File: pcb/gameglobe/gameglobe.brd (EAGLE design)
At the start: 99.1 x 49.5 mm, 14 parts

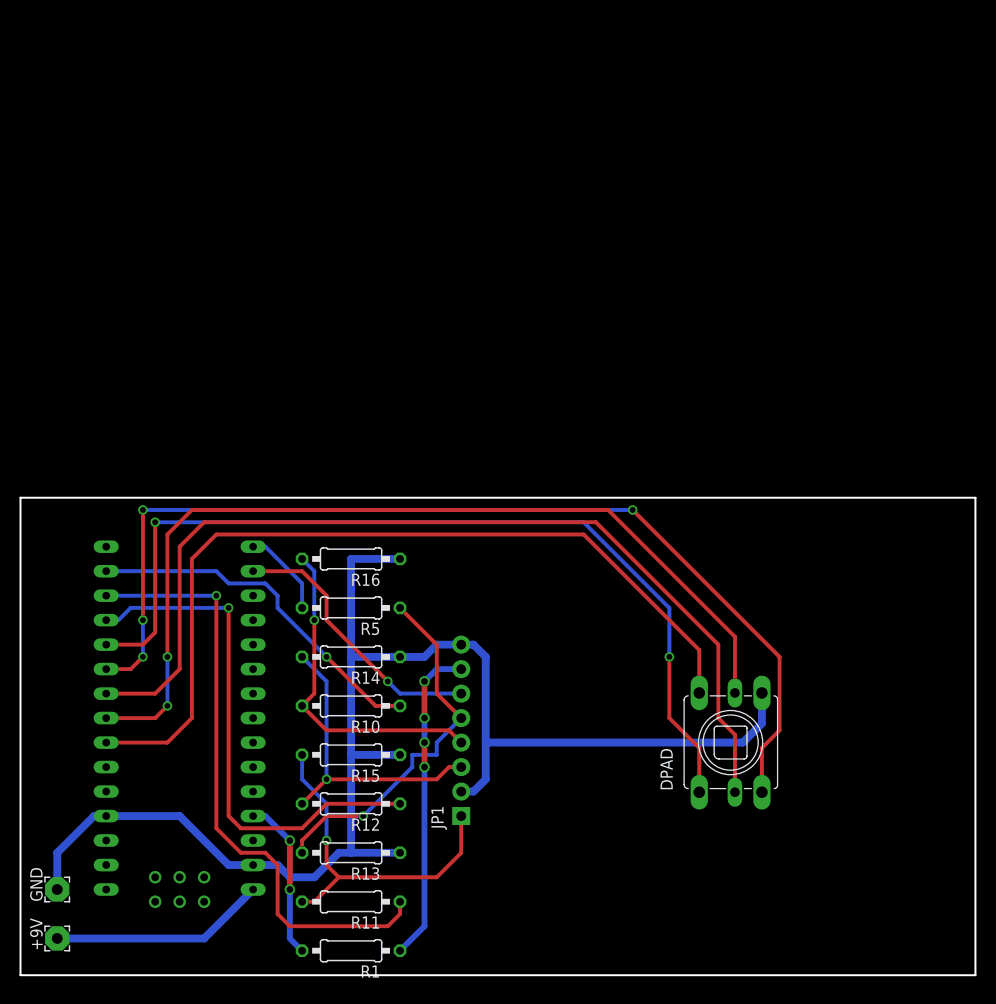
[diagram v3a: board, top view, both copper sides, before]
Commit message: Updated DRU file; Improved PCB layout; Added rounded edges and mount holes
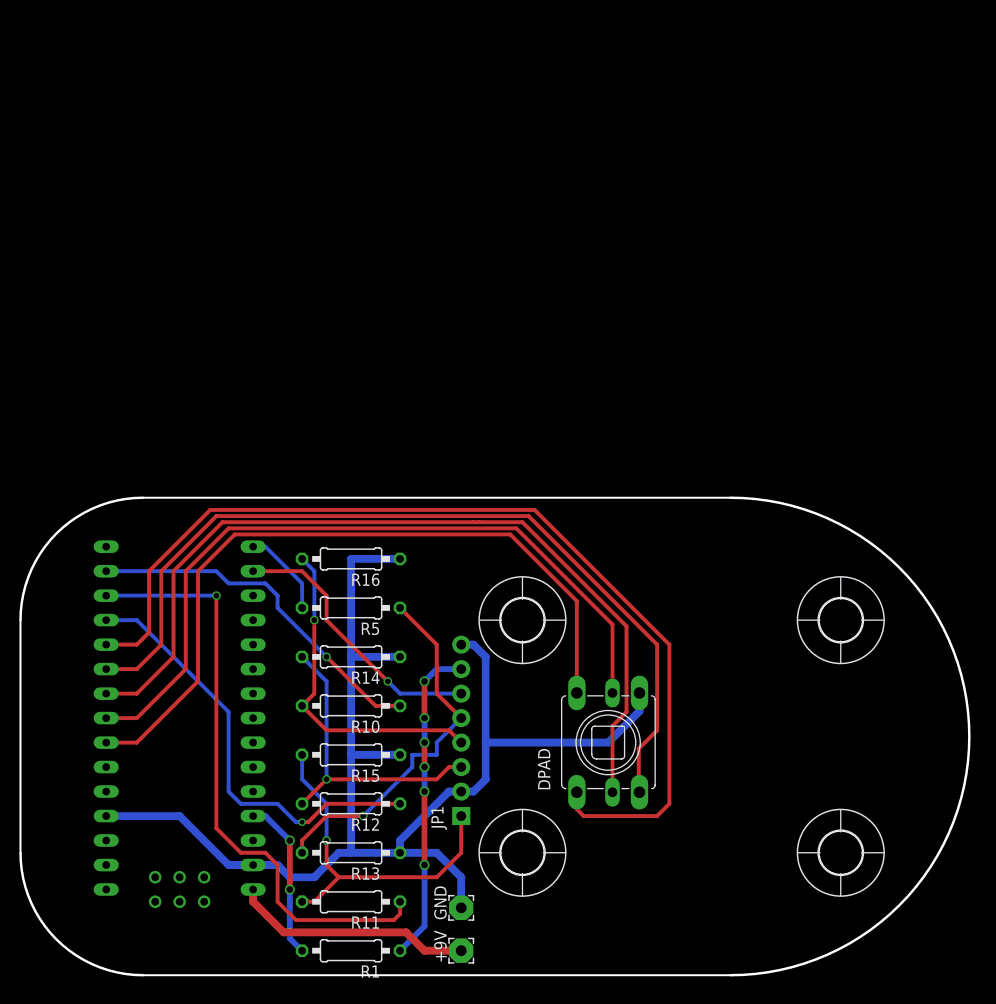
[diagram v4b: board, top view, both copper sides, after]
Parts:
- added ARDUINO_NANO: NANO, Arduino-clone:NANO
- added U$2, U$3, U$4: (no value), holes:4,5
- U$1: value NANO -> (none); device Arduino-clone:NANO -> holes:4,5
- moved GND 42.0 mm to (45.7, 6.99)
- moved +9V 41.9 mm to (45.7, 2.54)
- moved U$1 38.4 mm to (52.1, 12.7), flipped to the top
- moved DPAD 12.7 mm to (61.0, 24.1)
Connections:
- net DPAD_CENTER: now also ARDUINO_NANO.D4; no longer U$1.D4
- net DPAD_DOWN: now also ARDUINO_NANO.D7; no longer U$1.D7
- net DPAD_LEFT: now also ARDUINO_NANO.D6; no longer U$1.D6
- net DPAD_RIGHT: now also ARDUINO_NANO.D5; no longer U$1.D5
- net DPAD_UP: now also ARDUINO_NANO.D8; no longer U$1.D8
- net GND: now also ARDUINO_NANO.GND, ARDUINO_NANO.GND1; no longer U$1.GND, U$1.GND1
- net LCD_VCC: now also ARDUINO_NANO.3.3V; no longer U$1.3.3V
- net N$1: now also ARDUINO_NANO.D13; no longer U$1.D13
- net N$11: now also ARDUINO_NANO.5V; no longer U$1.5V
- net N$2: now also ARDUINO_NANO.D11; no longer U$1.D11
- net N$3: now also ARDUINO_NANO.D10; no longer U$1.D10
- net N$4: now also ARDUINO_NANO.D9; no longer U$1.D9
- net N$7: now also ARDUINO_NANO.RAW; no longer U$1.RAW
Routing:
- net DPAD_RIGHT: track 95.9 -> 77.9 mm, vias 2 -> 0
- net DPAD_DOWN: track 106.7 -> 89.8 mm, vias 4 -> 0
- net DPAD_CENTER: track 89.6 -> 76.9 mm
- net DPAD_LEFT: track 99.6 -> 88.8 mm
- net GND: track 148.7 -> 138.2 mm
- net N$4: track 54.2 -> 44.8 mm
- net DPAD_UP: track 94.5 -> 102.4 mm, vias 2 -> 0
- net N$7: track 22.4 -> 25.0 mm
- net N$3: track 63.6 -> 62.3 mm
- net LCD_LED: vias 4 -> 6
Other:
- board size 99.1 x 49.5 mm -> 98.4 x 49.5 mm
- board text added: "9V Battery"

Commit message: More PCB improvements, moved the Nano a bit sideways and improved battery mounting holes
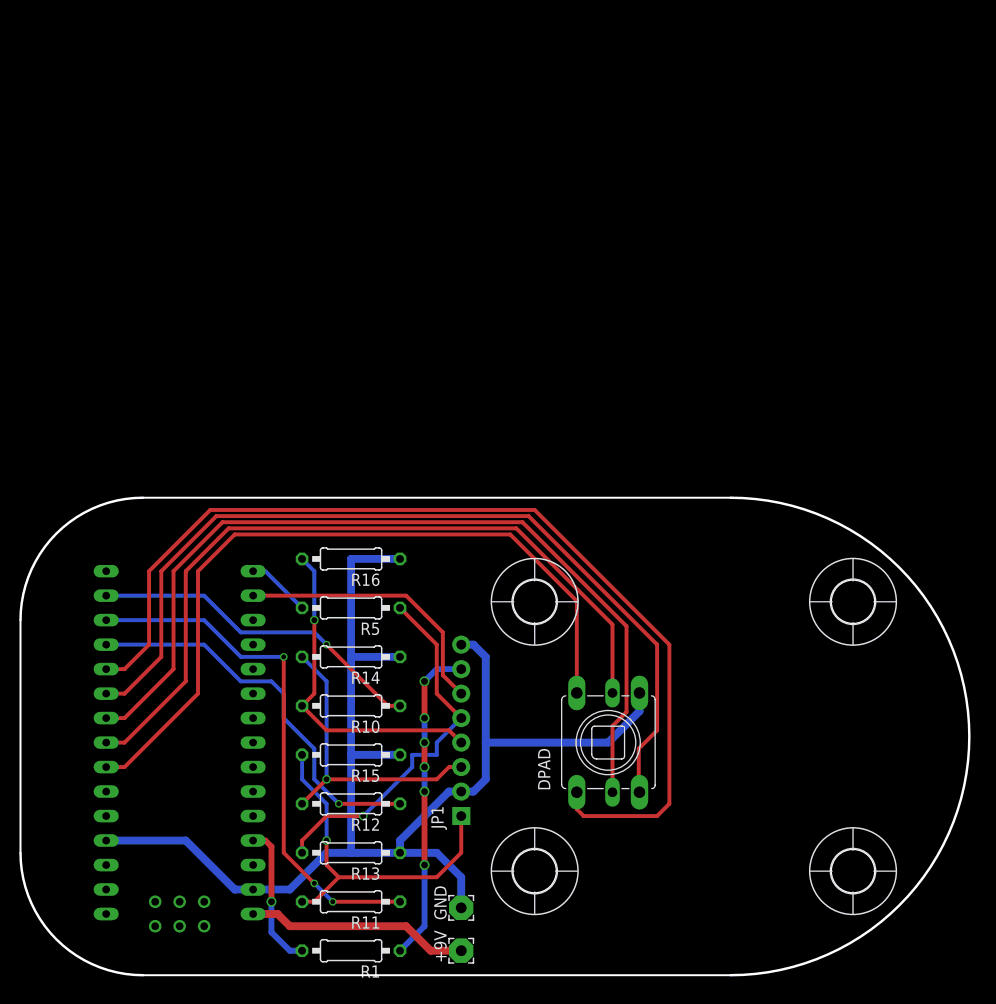
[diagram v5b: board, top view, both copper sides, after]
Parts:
- moved ARDUINO_NANO 2.54 mm to (14.0, 15.2)
- moved U$2 2.29 mm to (53.3, 38.7)
- moved U$1 2.29 mm to (53.3, 10.8)
- moved U$4 2.29 mm to (86.4, 38.7)
- moved U$3 2.29 mm to (86.4, 10.8)
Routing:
- net N$3: track 62.3 -> 54.5 mm, vias 1 -> 3
- net N$4: track 44.8 -> 40.7 mm
- net N$1: track 9.20 -> 6.66 mm
- net DPAD_UP: track 102.4 -> 104.2 mm
- net DPAD_RIGHT: track 77.9 -> 79.7 mm
- net DPAD_CENTER: track 76.9 -> 78.6 mm
- net N$7: track 25.0 -> 23.2 mm
- net N$11: track 16.8 -> 15.0 mm, vias 2 -> 1
- net DPAD_LEFT: track 88.8 -> 90.6 mm
- net DPAD_DOWN: track 89.8 -> 91.6 mm
- net N$2: track 37.0 -> 35.2 mm
- net LCD_VCC: track 28.3 -> 28.4 mm, vias 1 -> 0

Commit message: Many PCB improvements. Actually the first version where everything (joystick, lcd, nano) is centered on the board
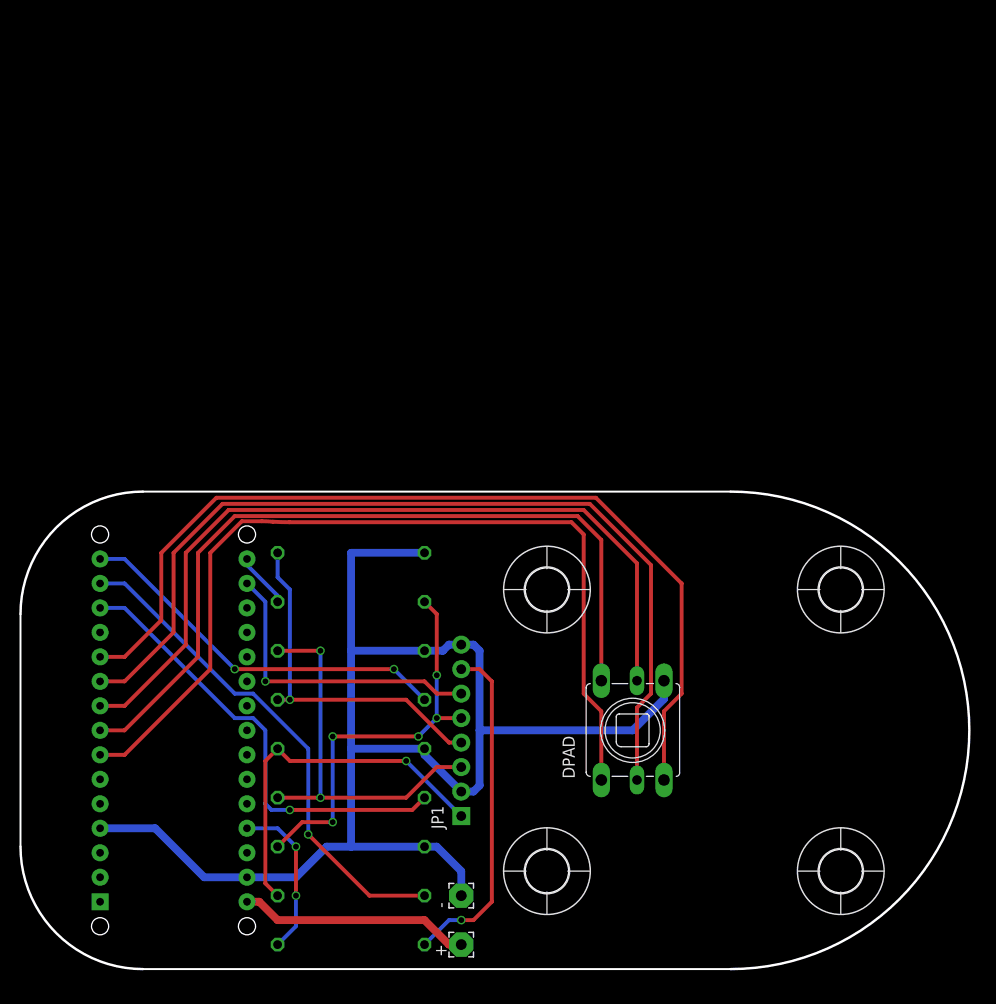
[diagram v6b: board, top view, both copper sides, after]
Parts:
- removed +9V, GND: WIREPAD2,54/1,1, wirepad:2,54/1,1
- removed ARDUINO_NANO: NANO, Arduino-clone:NANO
- added +, -: WIREPAD2,54/1,1, wirepad:2,54/1,1
- added U$5: ARDUINONANO, jet-lib:PDIP-32
- R1, R10, R11, R12, R13, R14, R15, R16, R5: device resistor:0207/10 -> resistor:0411/15
- moved DPAD 2.84 mm to (63.5, 25.4)
- moved U$2 1.80 mm to (54.6, 40.0)
- moved U$4 1.80 mm to (85.1, 40.0)
- moved U$1 1.27 mm to (54.6, 10.8)
- moved U$3 1.27 mm to (85.1, 10.8)
- moved R13 0.64 mm to (34.3, 13.3), flipped to the bottom, turned to 0 degrees
- moved R15 0.64 mm to (34.3, 23.5), flipped to the bottom, turned to 0 degrees
- moved R11 0.64 mm to (34.3, 8.26), flipped to the bottom, turned to 0 degrees
- moved R1 0.63 mm to (34.3, 3.17), flipped to the bottom, turned to 0 degrees
- moved R10 0.63 mm to (34.3, 28.6), flipped to the bottom, turned to 0 degrees
- moved R12 0.63 mm to (34.3, 18.4), flipped to the bottom, turned to 0 degrees
- moved R14 0.63 mm to (34.3, 33.7), flipped to the bottom, turned to 0 degrees
- moved R16 0.63 mm to (34.3, 43.8), flipped to the bottom, turned to 0 degrees
- moved R5 0.63 mm to (34.3, 38.7), flipped to the bottom, turned to 0 degrees
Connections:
- removed net DPAD_DOWN: ARDUINO_NANO.D7, DPAD.DOWN
- removed net DPAD_UP: ARDUINO_NANO.D8, DPAD.UP
- removed net LCD_VCC: ARDUINO_NANO.3.3V, JP1.6
- removed net N$11: ARDUINO_NANO.5V, R1.2
- new net 3V3: JP1.6, U$5.3V3
- new net 5V: R1.2, U$5.+5V
- new net N$5: DPAD.DOWN, U$5.D8
- new net N$6: DPAD.UP, U$5.D4
- net DPAD_CENTER: now also U$5.D5; no longer ARDUINO_NANO.D4
- net DPAD_LEFT: now also U$5.D7; no longer ARDUINO_NANO.D6
- net DPAD_RIGHT: now also U$5.D6; no longer ARDUINO_NANO.D5
- net GND: now also -.1, U$5.GND, U$5.GND1; no longer ARDUINO_NANO.GND, ARDUINO_NANO.GND1, GND.1
- net N$1: now also U$5.D13; no longer ARDUINO_NANO.D13
- net N$2: now also U$5.D12; no longer ARDUINO_NANO.D11
- net N$3: now also U$5.D11; no longer ARDUINO_NANO.D10
- net N$4: now also U$5.D10; no longer ARDUINO_NANO.D9
- net N$7: now also +.1, U$5.VIN; no longer +9V.1, ARDUINO_NANO.RAW
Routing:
- net DPAD_UP: track 104.2 -> 0.00 mm
- net N$5: track 0.00 -> 96.1 mm
- net N$6: track 0.00 -> 94.0 mm
- net DPAD_DOWN: track 91.6 -> 0.00 mm
- net 3V3: track 0.00 -> 31.8 mm, vias 0 -> 1
- net LCD_VCC: track 28.4 -> 0.00 mm
- net 5V: track 0.00 -> 16.8 mm, vias 0 -> 2
- net N$11: track 15.0 -> 0.00 mm, vias 1 -> 0
- net GND: track 138.2 -> 148.6 mm
- net LCD_DC: track 31.8 -> 40.1 mm, vias 1 -> 2
- net N$4: track 40.7 -> 47.3 mm
- net DPAD_LEFT: track 90.6 -> 95.1 mm
- net DPAD_CENTER: track 78.6 -> 83.2 mm
- net DPAD_RIGHT: track 79.7 -> 84.2 mm
- net N$2: track 35.2 -> 39.7 mm, vias 1 -> 2
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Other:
- board text added: "Arduino Nano"

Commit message: Fix and add own arduino Improve silkscreen texts
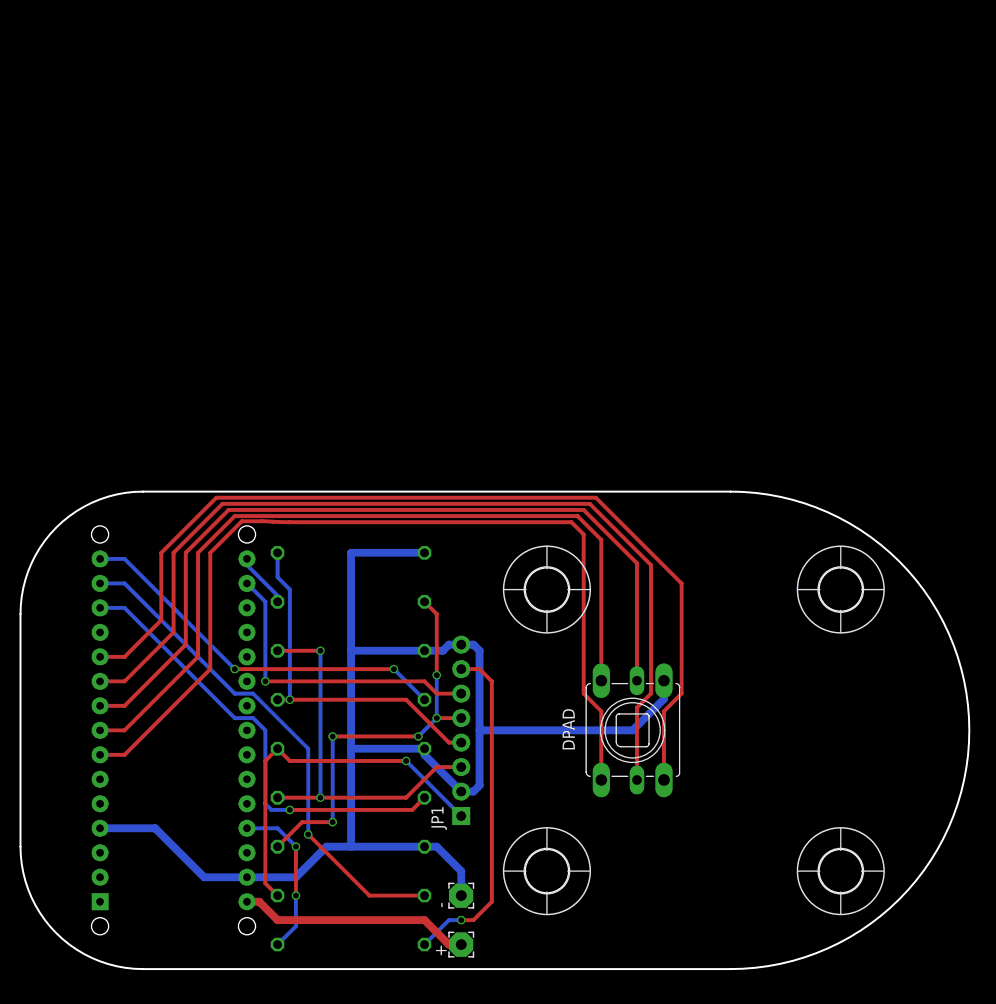
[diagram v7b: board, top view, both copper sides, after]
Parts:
- removed U$5: ARDUINONANO, jet-lib:PDIP-32
- added ARDUINO_NANO: ARDUINONANO, arduino_nano:PDIP-32
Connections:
- removed net N$5: DPAD.DOWN, U$5.D8
- removed net N$6: DPAD.UP, U$5.D4
- new net DPAD_DOWN: ARDUINO_NANO.D8, DPAD.DOWN
- new net DPAD_UP: ARDUINO_NANO.D4, DPAD.UP
- net 3V3: now also ARDUINO_NANO.3V3; no longer U$5.3V3
- net 5V: now also ARDUINO_NANO.+5V; no longer U$5.+5V
- net DPAD_CENTER: now also ARDUINO_NANO.D5; no longer U$5.D5
- net DPAD_LEFT: now also ARDUINO_NANO.D7; no longer U$5.D7
- net DPAD_RIGHT: now also ARDUINO_NANO.D6; no longer U$5.D6
- net GND: now also ARDUINO_NANO.GND, ARDUINO_NANO.GND1; no longer U$5.GND, U$5.GND1
- net N$1: now also ARDUINO_NANO.D13; no longer U$5.D13
- net N$2: now also ARDUINO_NANO.D12; no longer U$5.D12
- net N$3: now also ARDUINO_NANO.D11; no longer U$5.D11
- net N$4: now also ARDUINO_NANO.D10; no longer U$5.D10
- net N$7: now also ARDUINO_NANO.VIN; no longer U$5.VIN
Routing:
- net N$5: track 96.1 -> 0.00 mm
- net DPAD_DOWN: track 0.00 -> 96.1 mm
- net N$6: track 94.0 -> 0.00 mm
- net DPAD_UP: track 0.00 -> 94.0 mm
